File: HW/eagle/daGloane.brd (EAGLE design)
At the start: 100 x 80 mm, 89 parts, among them IC1 MCP1252-33X50, U1 STM32F10XTXU6, X2 SPARKFUN-CONNECTORS_USB-MICROB

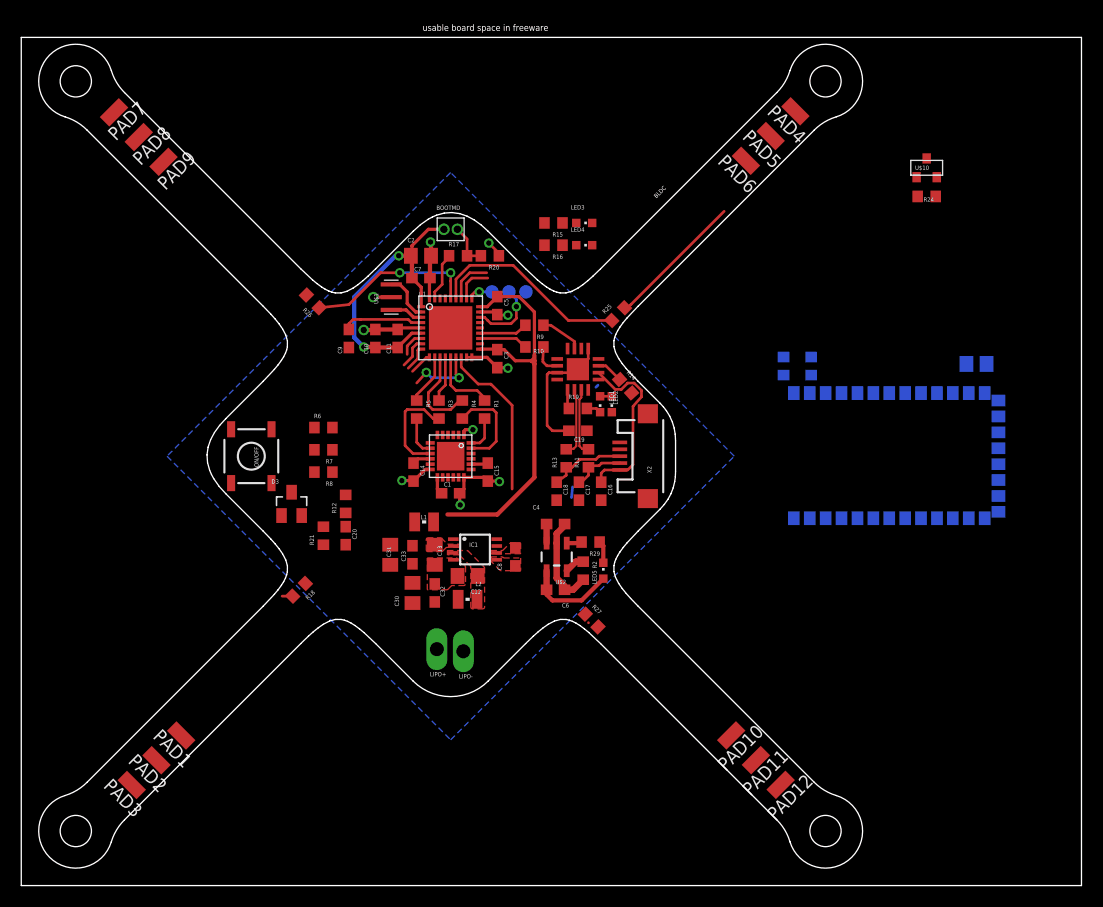
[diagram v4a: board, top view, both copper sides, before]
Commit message: voltage divider layout done
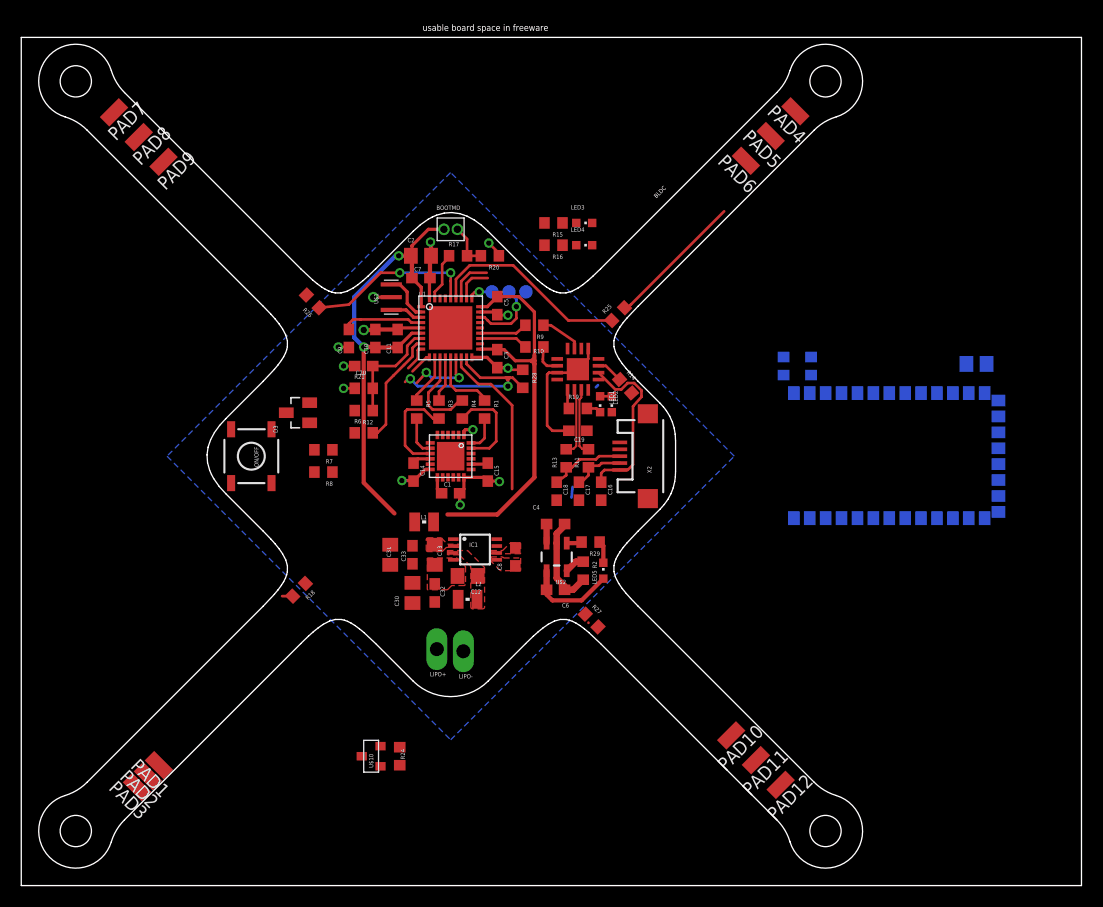
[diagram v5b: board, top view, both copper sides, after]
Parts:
- added R28: 10k, rcl:R0603
- moved U$10 76.3 mm to (33.0, 12.2), turned to 90 degrees
- moved R24 72.5 mm to (35.7, 12.2), turned to 270 degrees
- moved C20 16.1 mm to (32.3, 49.0), turned to 180 degrees
- moved R21 14.4 mm to (32.3, 46.9), turned to 0 degrees
- moved R12 8.96 mm to (32.3, 44.8), turned to 180 degrees
- moved D3 8.62 mm to (26.1, 44.6), turned to 90 degrees
- moved R6 3.83 mm to (32.3, 42.7)
- moved PAD1 3.50 mm to (13.0, 11.4)
- moved PAD2 1.70 mm to (12.0, 10.3)
- moved PAD3 0.54 mm to (10.9, 9.29)
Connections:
- net GND: now also R28.1; no longer U1.17
- net PWR_ON_µC: now also R28.2, U1.17; no longer U1.23
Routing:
- net PWR_ON_µC: track 0.00 -> 18.5 mm, vias 0 -> 2
- net VCC: track 67.3 -> 84.2 mm
- net VOLTAGE: track 2.41 -> 10.3 mm
- net PWR_OFF: track 2.92 -> 10.8 mm
- net GND: track 55.7 -> 59.8 mm, vias 10 -> 13

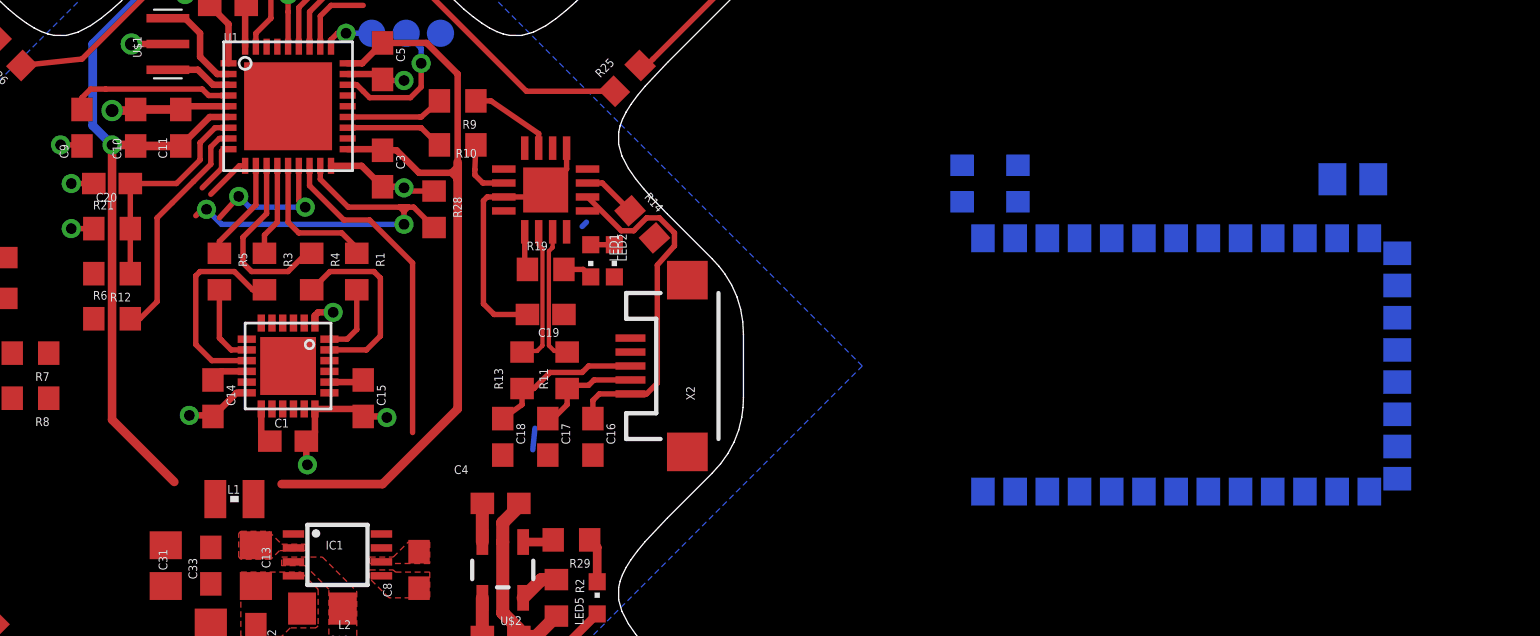
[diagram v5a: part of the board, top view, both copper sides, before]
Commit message: uart connection of bluetooth module routed
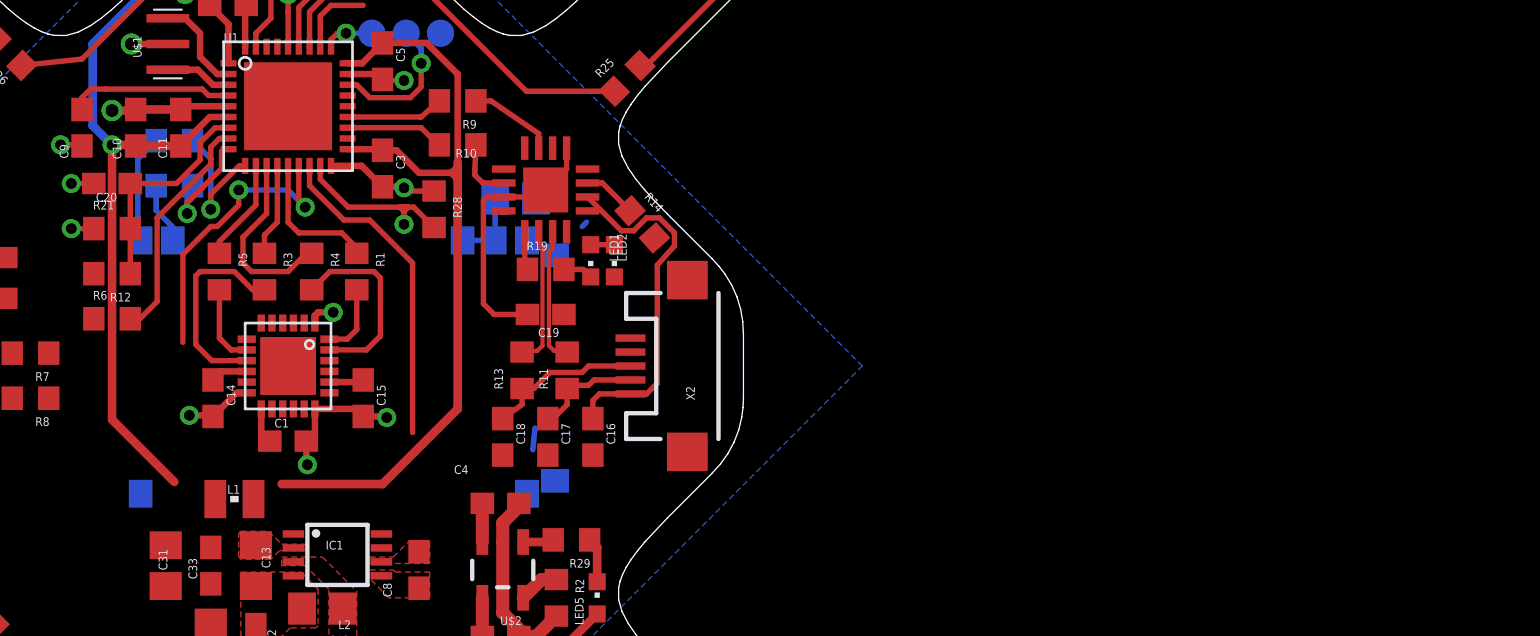
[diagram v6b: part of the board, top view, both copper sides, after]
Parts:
- U$5: value BLUETOOTH -> BLUETOOTH_REDUCED; device daGloane:BLUETOOTH -> daGloane:BLUETOOTH_REDUCED
- moved R23 39.3 mm to (35.2, 48.9), turned to 0 degrees
- moved C21 39.0 mm to (51.1, 48.3)
- moved R22 36.8 mm to (35.2, 51.0), turned to 0 degrees
- moved U$5 36.7 mm to (40.5, 40.6)
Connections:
- net VCC: now also U$5.P$34
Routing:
- net PWR_ON_µC: track 18.5 -> 8.42 mm, vias 2 -> 1
- net MOT1: track 6.70 -> 13.8 mm
- net N$7: track 0.00 -> 5.06 mm
- net USART2_RX: track 2.15 -> 6.40 mm, vias 0 -> 1
- net VCC: track 84.2 -> 87.6 mm
- net USART2_TX: track 2.44 -> 5.33 mm, vias 0 -> 1
- net N$15: track 0.00 -> 2.87 mm

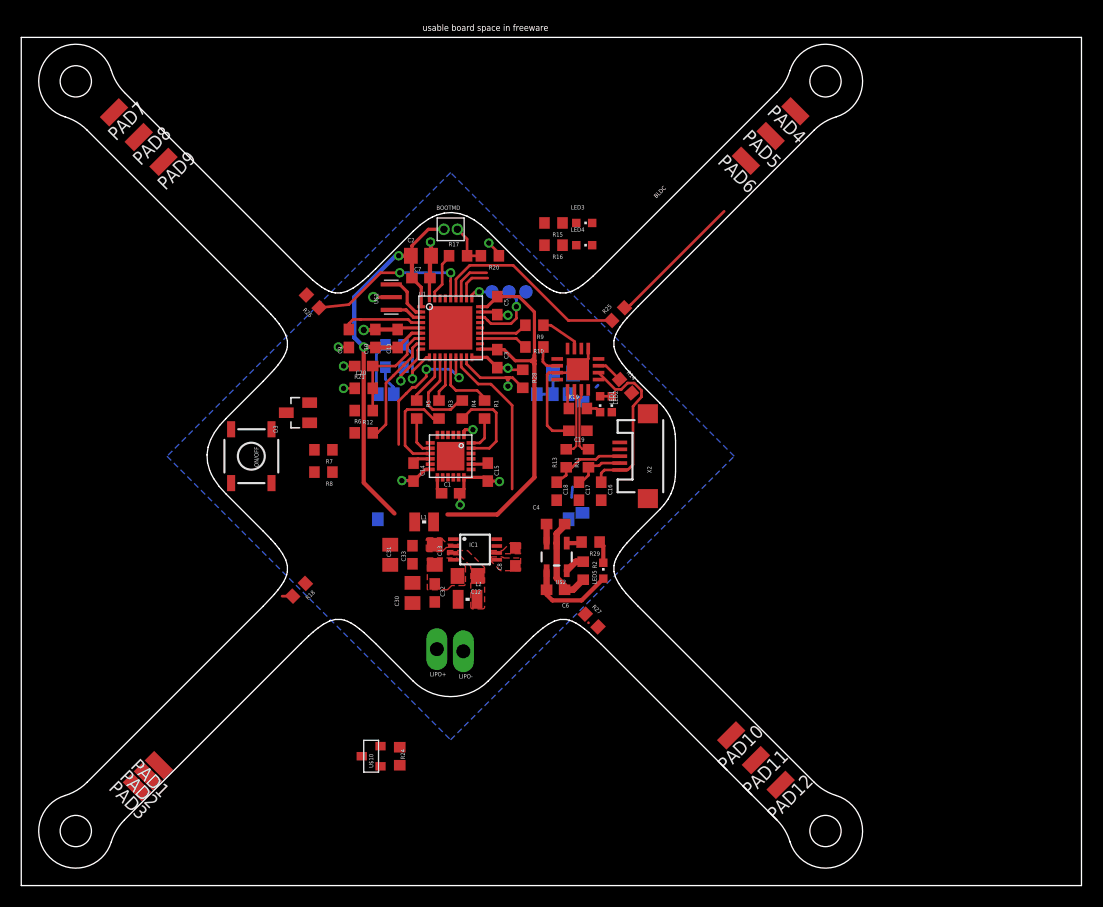
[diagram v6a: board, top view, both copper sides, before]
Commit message: FT230X layout finished BLDC power line layout started
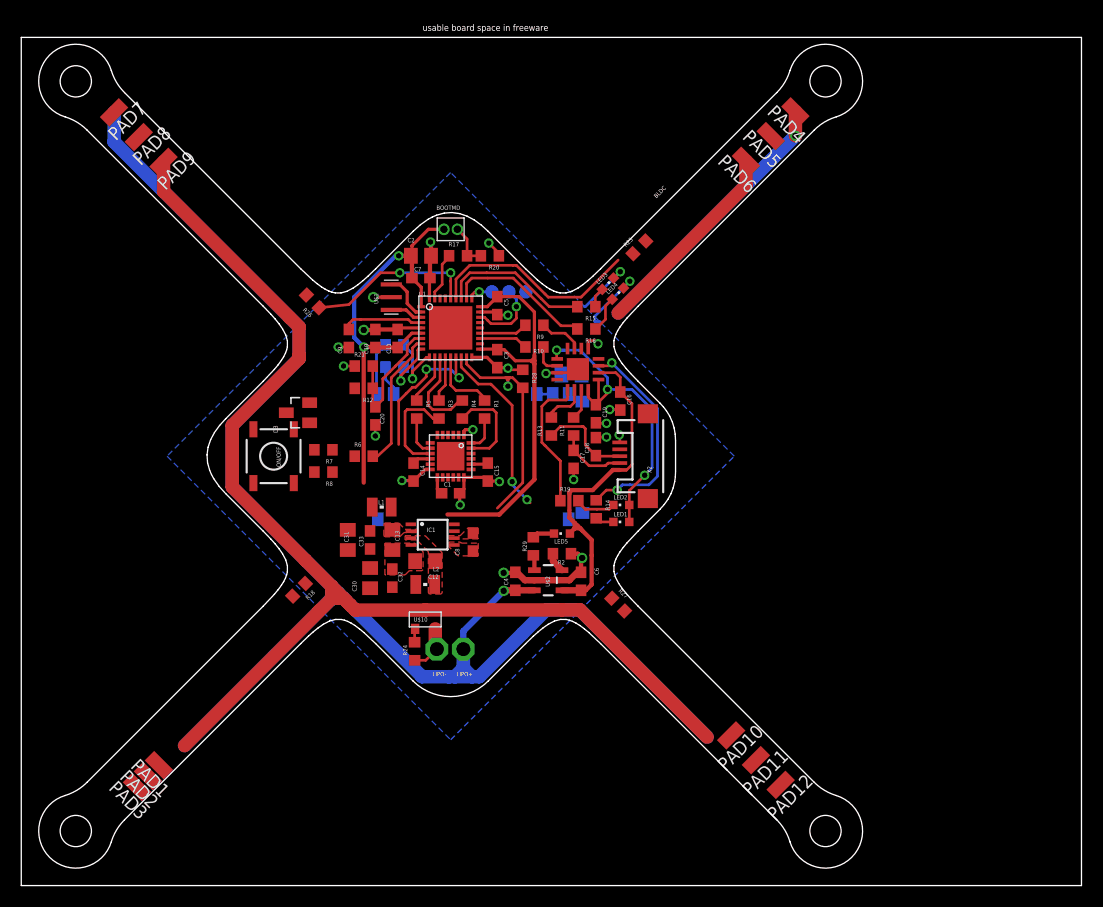
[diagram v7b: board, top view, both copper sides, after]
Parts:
- LIPO+, LIPO-: value TPSPAD1-13Y -> TPSPAD1-13; device testpad:P1-13Y -> testpad:P1-13
- moved U$10 13.9 mm to (38.1, 25.1), turned to 0 degrees
- moved R14 11.9 mm to (54.2, 35.5), turned to 270 degrees
- moved LED1 11.1 mm to (56.6, 34.3), turned to 90 degrees
- moved R24 10.00 mm to (37.1, 22.1), turned to 90 degrees
- moved LED2 9.71 mm to (56.6, 35.9), turned to 90 degrees
- moved R19 8.74 mm to (51.7, 36.3)
- moved C16 8.69 mm to (56.5, 45.7)
- moved R15 8.49 mm to (53.3, 54.6)
- moved R16 8.49 mm to (53.3, 52.5)
- moved R25 6.61 mm to (58.3, 60.2)
- moved C4 6.60 mm to (46.6, 28.7), turned to 90 degrees
- moved LED3 6.15 mm to (55.3, 56.8), turned to 315 degrees
- moved C18 5.60 mm to (54.2, 41.4), turned to 90 degrees
- moved LED4 5.56 mm to (56.3, 55.8), turned to 315 degrees
- moved R29 5.41 mm to (48.3, 32.0), turned to 270 degrees
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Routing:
- net LIPO: track 2.05 -> 168.5 mm, vias 0 -> 2
- net MOT_GND: track 0.00 -> 134.4 mm
- net VCCIO: track 1.38 -> 31.2 mm, vias 0 -> 3
- net N$11: track 2.52 -> 20.6 mm, vias 0 -> 2
- net GND: track 59.8 -> 74.7 mm, vias 13 -> 24
- net N$40: track 13.2 -> 0.00 mm
- net PWR_ON_µC: track 8.42 -> 20.8 mm
- net N$12: track 1.80 -> 13.2 mm
- net LED2: track 3.63 -> 14.1 mm
- net LED1: track 4.36 -> 14.2 mm
- net VBUS: track 25.4 -> 32.7 mm
- net VCC: track 87.6 -> 83.0 mm
- net N$9: track 0.00 -> 3.61 mm
- net N$16: track 6.35 -> 2.90 mm
- net N$1: track 1.39 -> 3.98 mm
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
